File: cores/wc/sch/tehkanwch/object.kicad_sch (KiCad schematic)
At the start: 4 parts

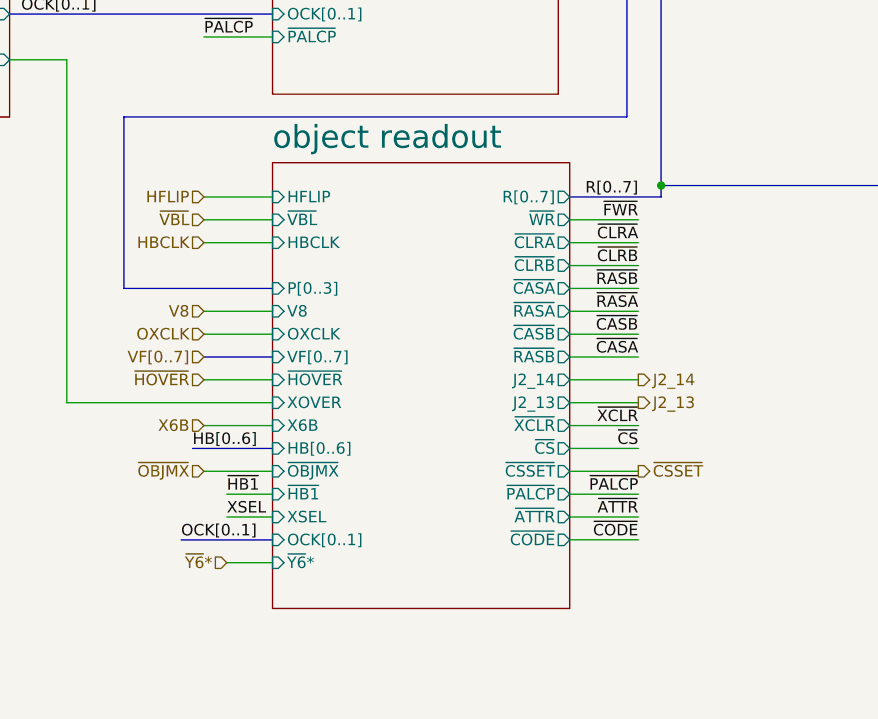
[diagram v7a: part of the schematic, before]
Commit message: wc: identified priority bit for fix layer
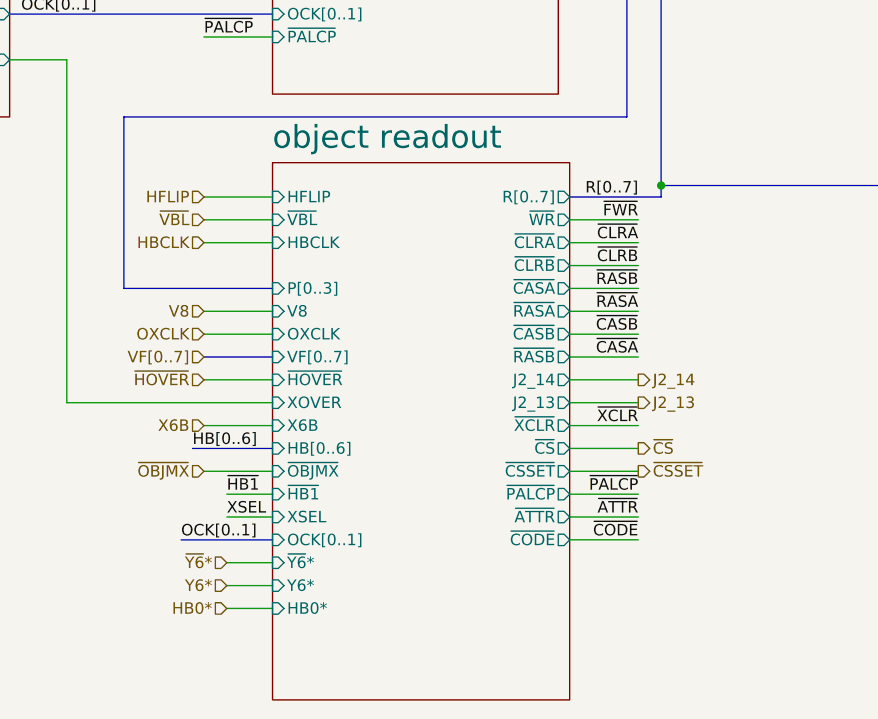
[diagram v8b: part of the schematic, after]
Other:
- sheet object readout ports: added HB0*, Y6*; removed none
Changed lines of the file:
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@@
 	(wire
 		(pts
+			(xy 142.24 203.2) (xy 147.32 203.2)
+		)
+		(stroke
+			(width 0)
+			(type default)
+		)
+	)
+	(wire
+		(pts
 			(xy 184.15 120.65) (xy 179.07 120.65)
 		)
@@
 	(wire
 		(pts
+			(xy 142.24 200.66) (xy 147.32 200.66)
+		)
+		(stroke
+			(width 0)
+			(type default)
+		)
+	)
+	(wire
+		(pts
 			(xy 295.91 128.27) (xy 300.99 128.27)
 		)
@@
 		)
 	)
-	(label "~{CS}"
-		(at 187.96 185.42 180)
-		(fields_autoplaced yes)
-		(effects
-			(font
-				(size 1.27 1.27)
-			)
-			(justify right bottom)
-		)
-	)
 	(label "HB1"
 		(at 81.28 138.43 0)
@@
 		)
 	)
+	(hierarchical_label "HB0*"
+		(shape input)
+		(at 142.24 203.2 180)
+		(fields_autoplaced yes)
+		(effects
+			(font
+				(size 1.27 1.27)
+			)
+			(justify right)
+		)
+	)
 	(hierarchical_label "~{CSSET}"
 		(shape output)
@@
 		)
 	)
+	(hierarchical_label "~{CS}"
+		(shape output)
+		(at 187.96 185.42 0)
+		(fields_autoplaced yes)
+		(effects
+			(font
+				(size 1.27 1.27)
+			)
+			(justify left)
+		)
+	)
 	(hierarchical_label "VF[0..7]"
 		(shape input)
@@
 		)
 	)
+	(hierarchical_label "Y6*"
+		(shape input)
+		(at 142.24 200.66 180)
+		(fields_autoplaced yes)
+		(effects
+			(font
+				(size 1.27 1.27)
+			)
+			(justify right)
+		)
+	)
 	(hierarchical_label "X6B"
 		(shape input)
@@
 	(sheet
 		(at 147.32 153.67)
-		(size 33.02 49.53)
+		(size 33.02 59.69)
 		(fields_autoplaced yes)
 		(stroke
@@
 		)
 		(property "Sheetfile" "objread.kicad_sch"
-			(at 147.32 203.7846 0)
+			(at 147.32 213.9446 0)
 			(effects
 				(font
@@
 			(effects
 				(font
+					(size 1.27 1.27)
+				)
+				(justify left)
+			)
+		)
+		(pin "HB0*" input
+			(at 147.32 203.2 180)
+			(effects
+				(font
+					(size 1.27 1.27)
+				)
+				(justify left)
+			)
+		)
+		(pin "Y6*" input
+			(at 147.32 200.66 180)
+			(effects
+				(font
